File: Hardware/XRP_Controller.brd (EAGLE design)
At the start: 63.5 x 54 mm, 194 parts, among them J1 POWER_JACKPOWER_JACK_SLOT, J12 Vertical Qwiic Connector, J13 Vertical Qwiic Connector, J14 Vertical Qwiic Connector, J3 JST_6_PIN_VERTICAL, J4 JST_6_PIN_VERTICAL, J5 JST_6_PIN_VERTICAL, J6 JST_6_PIN_VERTICAL, J9 Vertical Qwiic Connector, Q3 20V/4.2A/52mΩ/1.4W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

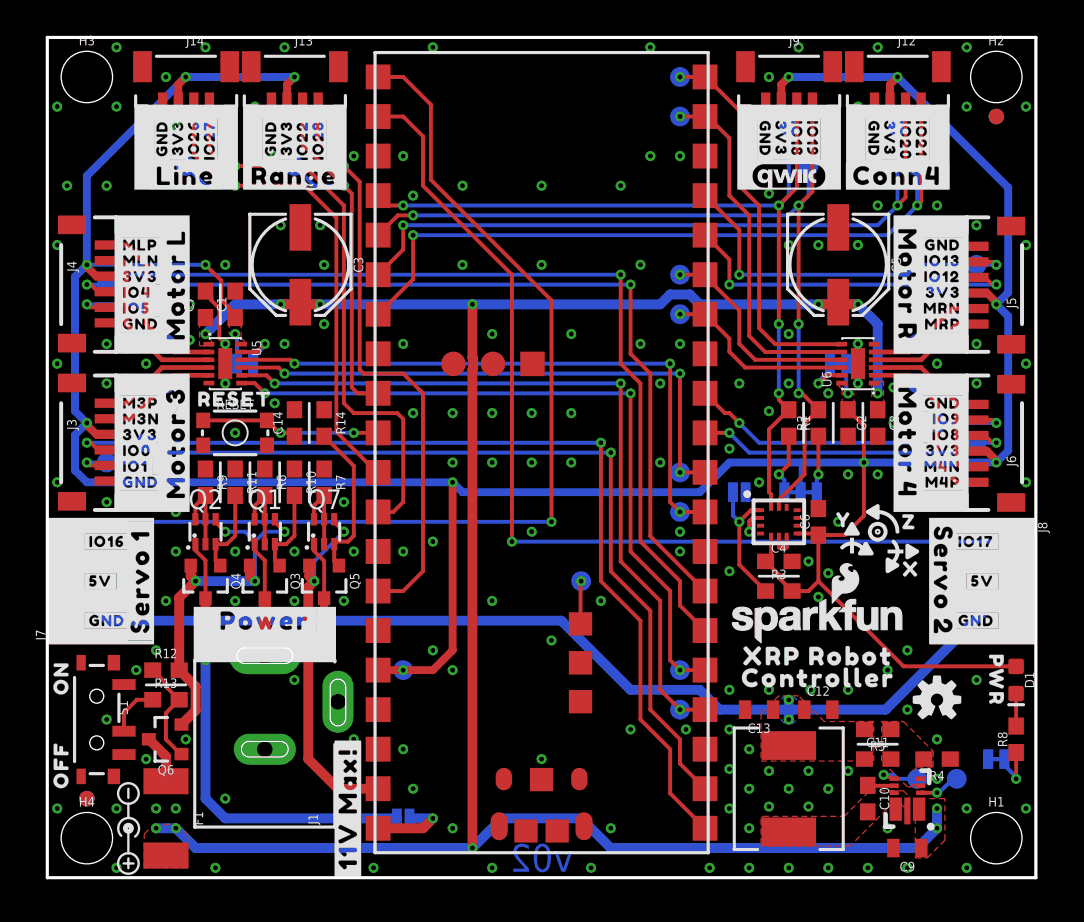
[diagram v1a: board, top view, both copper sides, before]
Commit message: Design review updates
Move version number in schematic to correct location
Rename 2nd expansion connector from "Range" to "Extra"
Rename 4th expansion connector from "Conn4" to "Range"
Add VIN measurement through voltage divider and NC jumper to IO28
Add V_BATT test point
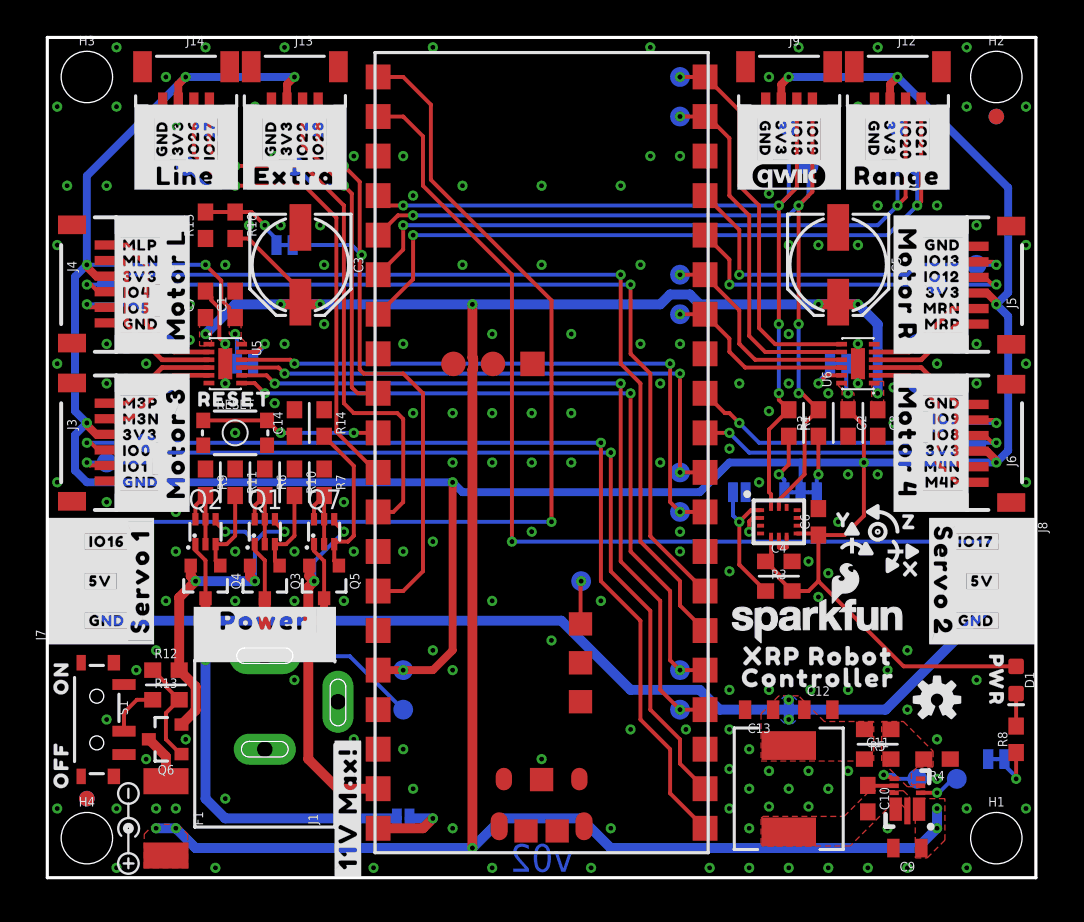
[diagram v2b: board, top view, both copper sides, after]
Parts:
- added R15: 33k, SparkFun-Resistors:0603
- added R16: 100k, SparkFun-Resistors:0603
- added TP37: TEST-POINT3X5, SparkFun-Connectors:PAD.03X.05
- added U$82: (no value), output:#EXTRA#0
- added VIN_MEAS: JUMPER-SMT_2_NC_TRACE_SILK, SparkFun-Jumpers:SMT-JUMPER_2_NC_TRACE_SILK
- U$13: device output:#CONN4#0 -> output:#VIN_MEAS#0
- moved U$13 40.5 mm to (14.4, 40.6), flipped to the bottom
- moved U$73 38.7 mm to (54.6, 45.1)
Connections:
- new net N$12: R15.2, R16.1, VIN_MEAS.2
- net GND: now also R15.1
- net RP_IO28: now also VIN_MEAS.1
- net VIN: now also R16.2
- net V_BATT: now also TP37.1
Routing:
- net V_BATT: track 7.47 -> 17.8 mm
- net VIN: track 143.8 -> 150.1 mm
- net N$12: track 0.00 -> 5.74 mm, vias 0 -> 1
- net RP_IO28: track 41.0 -> 45.8 mm, vias 1 -> 2
- net GND: vias 180 -> 181
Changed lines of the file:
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@@
 <rectangle x1="58.293" y1="18.542" x2="59.055" y2="19.558" layer="21"/>
 <rectangle x1="61.087" y1="14.986" x2="63.5" y2="23.114" layer="21"/>
-<rectangle x1="51.308" y1="44.323" x2="51.435" y2="45.847" layer="21"/>
-<rectangle x1="57.785" y1="44.323" x2="57.9628" y2="45.847" layer="21"/>
-<rectangle x1="51.308" y1="44.196" x2="57.9628" y2="44.323" layer="21"/>
+<rectangle x1="12.573" y1="44.323" x2="12.827" y2="45.847" layer="21"/>
+<rectangle x1="18.923" y1="44.323" x2="19.2278" y2="45.847" layer="21"/>
+<rectangle x1="12.573" y1="44.196" x2="19.2278" y2="44.323" layer="21"/>
 <rectangle x1="7.62" y1="23.495" x2="9.144" y2="24.003" layer="21"/>
 <rectangle x1="7.62" y1="31.877" x2="9.144" y2="32.385" layer="21"/>
@@
 <rectangle x1="13.843" y1="48.768" x2="17.907" y2="49.657" layer="21"/>
 <rectangle x1="13.843" y1="45.847" x2="17.907" y2="46.101" layer="21"/>
-<rectangle x1="12.573" y1="44.323" x2="12.7" y2="45.847" layer="21"/>
-<rectangle x1="19.05" y1="44.323" x2="19.2278" y2="45.847" layer="21"/>
-<rectangle x1="12.573" y1="44.196" x2="19.2278" y2="44.323" layer="21"/>
+<rectangle x1="51.308" y1="44.323" x2="51.435" y2="45.847" layer="21"/>
+<rectangle x1="57.785" y1="44.323" x2="57.9628" y2="45.847" layer="21"/>
+<rectangle x1="51.308" y1="44.196" x2="57.9628" y2="44.323" layer="21"/>
 <rectangle x1="10.922" y1="45.847" x2="12.2428" y2="49.657" layer="21"/>
 <rectangle x1="5.588" y1="45.847" x2="6.858" y2="49.657" layer="21"/>
@@
 <element name="U$6" library="output" package="PWR0" value="" x="60.96" y="12.7" smashed="yes" rot="R270"/>
 <element name="U$7" library="output" package="RESET0" value="" x="12.065" y="30.734" smashed="yes"/>
-<element name="U$13" library="output" package="#CONN4#0" value="" x="54.61" y="45.085" smashed="yes"/>
 <element name="U$4" library="output" package="#GND#0" value="" x="4.318" y="25.4" smashed="yes"/>
 <element name="U$15" library="output" package="#3V3#0" value="" x="4.318" y="28.448" smashed="yes"/>
@@
 <attribute name="VALUE" x="16.68" y="19.525" size="1.27" layer="27"/>
 </element>
-<element name="U$73" library="output" package="#RANGE#0" value="" x="15.875" y="45.085" smashed="yes"/>
+<element name="U$73" library="output" package="#RANGE#0" value="" x="54.61" y="45.085" smashed="yes"/>
 <element name="U$74" library="output" package="#LINE#0" value="" x="8.89" y="45.085" smashed="yes"/>
 <element name="U$10" library="output" package="#MOTOR_L#0" value="" x="8.255" y="38.1" smashed="yes" rot="R90"/>
@@
 <element name="U$80" library="output" package="Y0" value="" x="55.88" y="22.86" smashed="yes" rot="MR0"/>
 <element name="U$81" library="output" package="Z0" value="" x="51.435" y="23.368" smashed="yes" rot="MR0"/>
+<element name="U$82" library="output" package="#EXTRA#0" value="" x="15.875" y="45.085" smashed="yes"/>
+<element name="R16" library="SparkFun-Resistors" package="0603" value="100k" x="12.065" y="41.91" smashed="yes" rot="R270">
+<attribute name="NAME" x="12.827" y="41.91" size="0.6096" layer="25" font="vector" ratio="20" rot="R270" align="bottom-center"/>
+<attribute name="PROD_ID" value="RES-07828" x="12.065" y="41.91" size="1.778" layer="27" rot="R270" display="off"/>
+<attribute name="VALUE" x="11.303" y="41.91" size="0.6096" layer="27" font="vector" ratio="20" rot="R270" align="top-center"/>
+</element>
+<element name="VIN_MEAS" library="SparkFun-Jumpers" package="SMT-JUMPER_2_NC_TRACE_SILK" package3d_urn="urn:adsk.eagle:package:39281/1" value="JUMPER-SMT_2_NC_TRACE_SILK" x="15.24" y="40.64" smashed="yes" rot="MR0">
+<attribute name="NAME" x="15.24" y="41.783" size="0.6096" layer="26" font="vector" ratio="20" rot="MR0" align="bottom-center"/>
+<attribute name="VALUE" x="15.24" y="39.497" size="0.6096" layer="28" font="vector" ratio="20" rot="MR0" align="top-center"/>
+</element>
+<element name="R15" library="SparkFun-Resistors" package="0603" value="33k" x="10.16" y="41.91" smashed="yes" rot="R90">
+<attribute name="NAME" x="9.398" y="41.91" size="0.6096" layer="25" font="vector" ratio="20" rot="R90" align="bottom-center"/>
+<attribute name="PROD_ID" value="RES-08416" x="10.16" y="41.91" size="1.778" layer="27" rot="R90" display="off"/>
+<attribute name="VALUE" x="10.922" y="41.91" size="0.6096" layer="27" font="vector" ratio="20" rot="R90" align="top-center"/>
+</element>
+<element name="U$13" library="output" package="#VIN_MEAS#0" value="" x="14.351" y="40.64" smashed="yes" rot="MR0"/>
+<element name="TP37" library="SparkFun-Connectors" package="PAD.03X.05" value="TEST-POINT3X5" x="22.86" y="10.795" smashed="yes" rot="MR0"/>
 </elements>
 <signals>
@@
 <via x="14.605" y="46.355" extent="1-16" drill="0.3048"/>
 <via x="8.255" y="48.26" extent="1-16" drill="0.3048"/>
+<contactref element="R15" pad="1"/>
+<via x="12.954" y="41.91" extent="1-16" drill="0.3048"/>
 </signal>
 <signal name="3.3V">
@@
 <wire x1="13.97" y1="17.95" x2="13.97" y2="20.38105" width="0.254" layer="1"/>
 <wire x1="13.97" y1="14.224" x2="13.97" y2="17.95" width="0.762" layer="1"/>
+<contactref element="TP37" pad="1"/>
+<wire x1="13.97" y1="14.224" x2="19.431" y2="14.224" width="0.254" layer="16"/>
+<wire x1="19.431" y1="14.224" x2="22.86" y2="10.795" width="0.254" layer="16"/>
 </signal>
 <signal name="RP_IO2/MOT_3_PH">
@@
 <wire x1="22.86" y1="18.415" x2="24.13" y2="19.685" width="0.254" layer="1"/>
 <wire x1="24.13" y1="19.685" x2="24.13" y2="31.115" width="0.254" layer="1"/>
-<wire x1="20.32" y1="32.385" x2="20.066" y2="32.639" width="0.254" layer="1"/>
+<wire x1="20.066" y1="32.639" x2="20.32" y2="32.385" width="0.254" layer="1"/>
 <wire x1="22.86" y1="32.385" x2="20.32" y2="32.385" width="0.254" layer="1"/>
-<wire x1="20.066" y1="32.639" x2="20.066" y2="44.704" width="0.254" layer="1"/>
 <contactref element="J13" pad="4"/>
 <wire x1="17.397" y1="47.373" x2="17.397" y2="49.67" width="0.254" layer="1"/>
-<wire x1="20.066" y1="44.704" x2="19.05" y2="45.72" width="0.254" layer="1"/>
+<wire x1="19.05" y1="45.72" x2="20.066" y2="44.704" width="0.254" layer="1"/>
 <contactref element="TP24" pad="1"/>
 <wire x1="19.05" y1="45.72" x2="17.397" y2="47.373" width="0.254" layer="1"/>
@@
 <wire x1="19.05" y1="45.72" x2="19.05" y2="46.355" width="0.254" layer="16"/>
 <wire x1="19.05" y1="46.355" x2="17.145" y2="48.26" width="0.254" layer="16"/>
+<contactref element="VIN_MEAS" pad="1"/>
+<wire x1="15.7607" y1="40.64" x2="19.558" y2="40.64" width="0.254" layer="16"/>
+<wire x1="19.558" y1="40.64" x2="20.193" y2="40.005" width="0.254" layer="16"/>
+<via x="20.193" y="40.005" extent="1-16" drill="0.3048"/>
+<wire x1="20.193" y1="40.005" x2="20.066" y2="39.878" width="0.254" layer="1"/>
+<wire x1="20.066" y1="39.878" x2="20.066" y2="32.639" width="0.254" layer="1"/>
+<wire x1="20.066" y1="40.132" x2="20.193" y2="40.005" width="0.254" layer="1"/>
+<wire x1="20.066" y1="44.704" x2="20.066" y2="40.132" width="0.254" layer="1"/>
 </signal>
 <signal name="RP_IO4/ENC_L_A">
@@
 <wire x1="41.275" y1="37.465" x2="41.91" y2="36.83" width="0.635" layer="16"/>
 <wire x1="40.005" y1="37.465" x2="41.275" y2="37.465" width="0.635" layer="16"/>
+<contactref element="R16" pad="2"/>
+<wire x1="16.256" y1="36.97" x2="16.256" y2="37.719" width="0.254" layer="1"/>
+<wire x1="12.915" y1="41.06" x2="12.065" y2="41.06" width="0.254" layer="1"/>
+<wire x1="16.256" y1="37.719" x2="12.915" y2="41.06" width="0.254" layer="1"/>
 </signal>
 <signal name="N$8">
@@
 <wire x1="21.25" y1="5.715" x2="18.669" y2="5.715" width="0.635" layer="1"/>
 </signal>
+<signal name="N$12">
+<contactref element="R16" pad="1"/>
+<contactref element="VIN_MEAS" pad="2"/>
+<contactref element="R15" pad="2"/>
+<wire x1="10.16" y1="42.76" x2="12.065" y2="42.76" width="0.254" layer="1"/>
+<wire x1="14.7193" y1="40.64" x2="14.7193" y2="41.021" width="0.254" layer="16"/>
+<wire x1="14.7193" y1="41.021" x2="13.97" y2="41.7703" width="0.254" layer="16"/>
+<wire x1="13.97" y1="41.7703" x2="13.97" y2="41.91" width="0.254" layer="16"/>
+<via x="13.97" y="41.91" extent="1-16" drill="0.3048"/>
+<wire x1="13.97" y1="41.91" x2="13.12" y2="42.76" width="0.254" layer="1"/>
+<wire x1="13.12" y1="42.76" x2="12.065" y2="42.76" width="0.254" layer="1"/>
+</signal>
 </signals>

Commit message: Design review updates
Schematic:
Restore Q6 value
Add user button to IO22 via NC jumper
Move USB_POW next to Pico W
Add current limiting resistor to VUSB

Board:
Place user button at top left corner
Move USB_POW jumper under barrel connector
Nudge V_SYS trace to get better GND pour
Reduce selective solder path widths
Move test points away from middle to make room for logos (BOOTSEL, V_BATT, 3.3V, MOT_3_PH/EN)
Add vias to power traces for less voltage drop
Update vertical Qwiic connector footprint
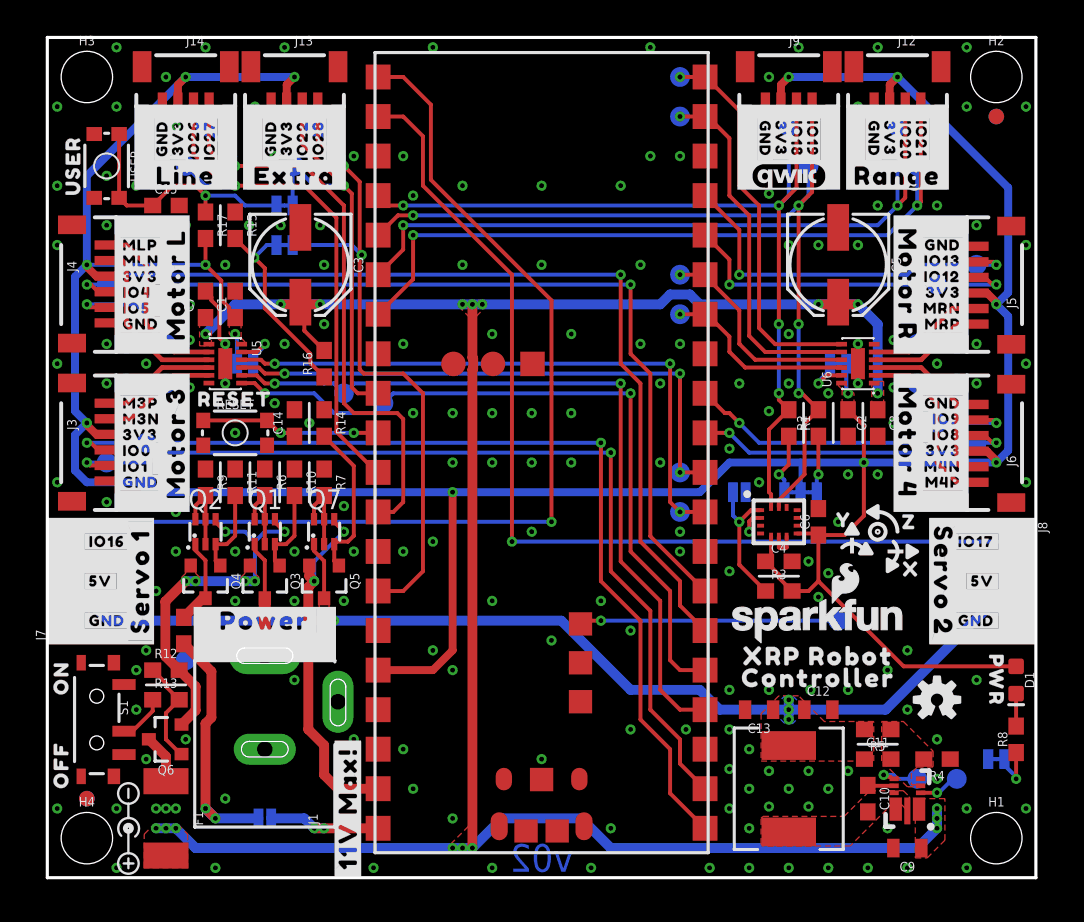
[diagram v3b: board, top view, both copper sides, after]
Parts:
- added C15: 0.1uF, SparkFun-Capacitors:0603
- added R17: 100k, SparkFun-Resistors:0603
- added R18: 4.7, SparkFun-Resistors:0603
- added U$83: (no value), output:USER0
- added U$84: (no value), output:#USER_BTN#0
- added USER: MOMENTARY-SWITCH-SPST-SMD-4.6X2.8MM, SparkFun-Switches:TACTILE_SWITCH_SMD_4.6X2.8MM
- added USER_BTN: JUMPER-SMT_2_NC_TRACE_SILK, SparkFun-Jumpers:SMT-JUMPER_2_NC_TRACE_SILK
- moved TP3 29.6 mm to (19.1, 31.1)
- moved TP4 25.6 mm to (21.6, 30.5)
- moved TP33 20.4 mm to (6.35, 25.4)
- moved TP36 16.7 mm to (50.8, 16.5)
- moved TP37 14.3 mm to (8.89, 14.0)
- moved R16 10.6 mm to (17.8, 33.0), turned to 90 degrees
- moved USB_POW 8.89 mm to (14.0, 3.81)
- moved U$65 7.37 mm to (14.7, 3.81)
- moved R15 1.90 mm to (12.1, 41.9), turned to 270 degrees
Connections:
- new net N$17: C15.1, R17.1, USER.3, USER.4, USER_BTN.1
- new net N$18: R18.2, USB_POW.2
- net 3.3V: now also R17.2
- net GND: now also C15.2, USER.1, USER.2
- net N$9: now also U1.40, USB_POW.1; no longer Q2.1, Q4.3, USB_POW.2
- net RP_IO22: now also USER_BTN.2
- net V_USB: now also Q2.1, Q4.3, R18.1; no longer U1.40, USB_POW.1
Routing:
- net N$9: track 29.4 -> 7.77 mm, vias 1 -> 2
- net N$17: track 0.00 -> 16.5 mm, vias 0 -> 1
- net N$18: track 0.00 -> 16.0 mm, vias 0 -> 2
- net BOOTSEL: track 2.76 -> 16.6 mm
- net N$12: track 5.74 -> 13.0 mm
- net V_BATT: track 17.8 -> 12.7 mm
- net RP_IO22: track 25.0 -> 27.6 mm
- net VIN: track 150.1 -> 147.5 mm, vias 12 -> 18
- net 5V: track 74.0 -> 72.6 mm, vias 3 -> 5
- net V_POW: track 25.5 -> 24.4 mm, vias 4 -> 6
- net 3.3V: track 216.5 -> 217.6 mm, vias 14 -> 13
- net RP_IO3/MOT_3_EN: track 46.0 -> 47.0 mm, vias 3 -> 2
- net RP_IO2/MOT_3_PH: track 48.7 -> 49.2 mm, vias 3 -> 2
- net V_USB: track 5.28 -> 5.65 mm, vias 1 -> 0
- net GND: vias 181 -> 190
- added copper zone on layer 1, net V_POW

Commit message: v10 updates
Bump version number to v10
Update Pico W datasheet
Change Pico W footprint to match datasheet recommendations
Nudge inner expansion connectors inwards to be on 0.05" grid
Rename USB_POW jumper to VUSB
Replace PWR_LED jumper silk label with PWR
Add XRP logos
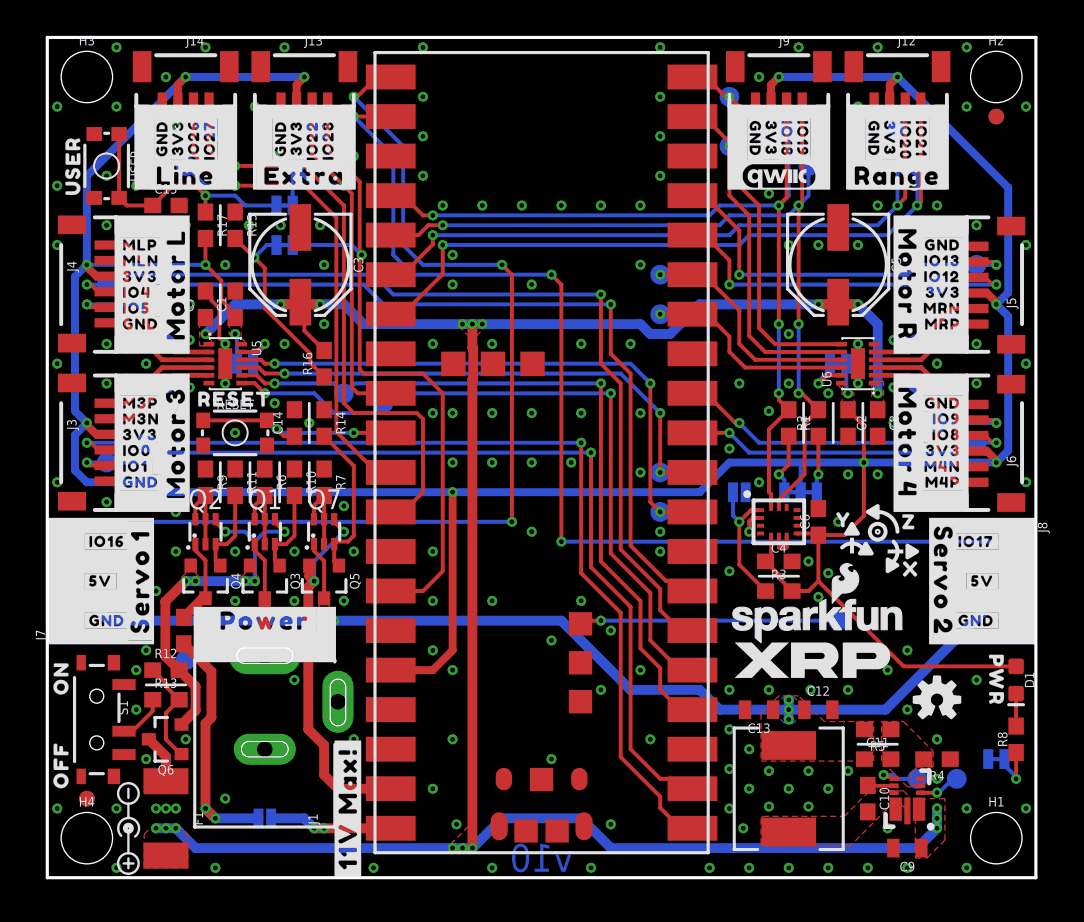
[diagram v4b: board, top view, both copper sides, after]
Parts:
- removed U$68: (no value), output:#PWR_LED#0
- removed U$69, U$71: (no value), output:XRP_ROBOT0
- removed U$70, U$72: (no value), output:CONTROLLER0
- added U$85: (no value), output:0X6B0
- added U$86: (no value), output:0X6A0
- added U$87: (no value), output:OPEN#0
- added U$91: (no value), output:CLOSED#0
- added U$92: (no value), XRP_LOGOS:XRP_FULL_LOGO
- added U$93: (no value), output:#VUSB#0
- added U$94: (no value), output:#PWR#0
- LOGO3: value SFE_LOGO_NAME_FLAME.1_INCH -> SFE_LOGO_NAME_FLAME.3_INCH; device SparkFun-Aesthetics:SFE_LOGO_NAME_FLAME_.1 -> SparkFun-Aesthetics:SFE_LOGO_NAME_FLAME_.3
- U$65: device output:#USB_POW#0 -> XRP_LOGOS:XRP_LOGO
- moved U$65 35.9 mm to (49.1, 14.0), flipped to the top
- moved LOGO3 8.54 mm to (37.5, 41.9)
- moved TP15 3.70 mm to (43.8, 47.0)
- moved TP16 3.42 mm to (43.8, 50.2)
- moved TP11 1.27 mm to (39.4, 36.2)
- moved TP12 1.27 mm to (39.4, 38.7)
- moved TP7 1.27 mm to (39.4, 23.5)
- moved TP8 1.27 mm to (39.4, 26.0)
- moved U$46 0.64 mm to (47.5, 49.1)
- moved J13 0.64 mm to (16.5, 48.9)
- moved U$45 0.64 mm to (17.0, 49.1)
- moved U$82 0.64 mm to (16.5, 45.1)
- moved U$42 0.63 mm to (15.0, 49.1)
- moved J9 0.63 mm to (47.0, 48.9)
- moved U$39 0.63 mm to (18.0, 49.1)
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- renumbered USB_POW to VUSB
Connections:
- net RP_IO20 renamed RP_IO20/RANGE_TRIG
- net RP_IO21 renamed RP_IO21/RANGE_ECHO
- net RP_IO22 renamed RP_IO22/USER_BTN
- net RP_IO26 renamed RP_IO26/LINE_L
- net RP_IO27 renamed RP_IO27/LINE_R
- net RP_IO28 renamed RP_IO28/VIN_MEAS
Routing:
- net RP_IO17/S2_OUT: track 64.3 -> 69.7 mm, vias 1 -> 3
- net RP_IO7/MOT_L_EN: track 36.3 -> 34.0 mm
- net RP_IO6/MOT_L_PH: track 39.0 -> 37.5 mm
- net RP_IO3/MOT_3_EN: track 47.0 -> 45.5 mm
- net RP_IO2/MOT_3_PH: track 49.2 -> 47.7 mm
- net RP_IO28/VIN_MEAS: track 45.8 -> 47.3 mm
- net RP_IO4/ENC_L_A: track 61.1 -> 59.7 mm
- net RP_IO21/RANGE_ECHO: track 48.3 -> 46.9 mm
- net RP_IO20/RANGE_TRIG: track 47.9 -> 46.5 mm
- net RP_IO27/LINE_R: track 40.5 -> 41.9 mm
- net RP_IO10/MOT_4_PH: track 12.4 -> 13.6 mm
- net RP_IO11/MOT_4_EN: track 14.0 -> 15.2 mm
- net RP_IO5/ENC_L_B: track 58.5 -> 57.3 mm
- net !RP_RESET!: track 12.5 -> 13.7 mm
- net RP_IO19/SCL: track 58.5 -> 57.5 mm
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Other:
- board text added: "v10"
- board text removed: "v02"
